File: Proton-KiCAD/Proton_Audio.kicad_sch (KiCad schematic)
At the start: 30 parts, among them J13 SJ-43514, J15 SPEAKER_OUT, U10 LM324, U9 LM386

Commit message: finished updated layout
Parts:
- J6: renamed from J13; footprint Custom_footprints:CUI_SJ-43514 -> Custom Footprints:CUI_SJ-43514
- renumbered C28 to C24, C22 to C25, C36 to C26, C37 to C27, C38 to C28, C23 to C29, C24 to C30, C39 to C31, C25 to C32, C40 to C33, C42 to C34, C43 to C35, J15 to J12, R44 to R19, R45 to R20, R25 to R22, R38 to R27, R39 to R28, R35 to R29, R15 to R30, R36 to R31, R26 to R32, R27 to R33, R37 to R34, R28 to R35, R42 to R38, U10 to U6, U9 to U7
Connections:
- net VGND is gone; now on net SGND: C26.2, C27.2, C29.2, C31.2, C32.2, R30.1
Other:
- moved on the sheet: C33, C34, C35, J12, R38, U7

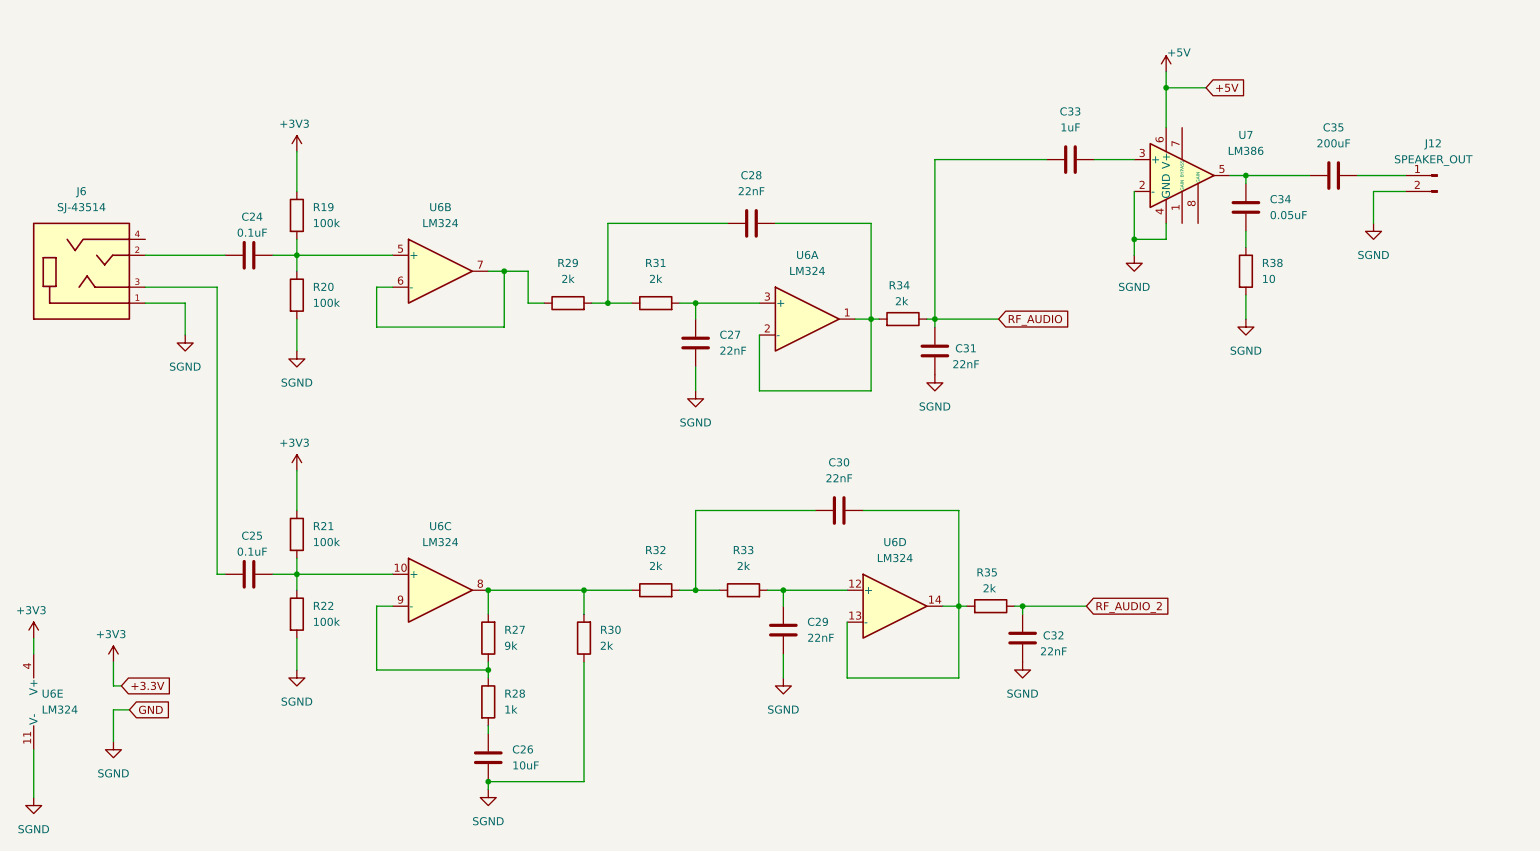
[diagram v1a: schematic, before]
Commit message: BOM and CPL changes
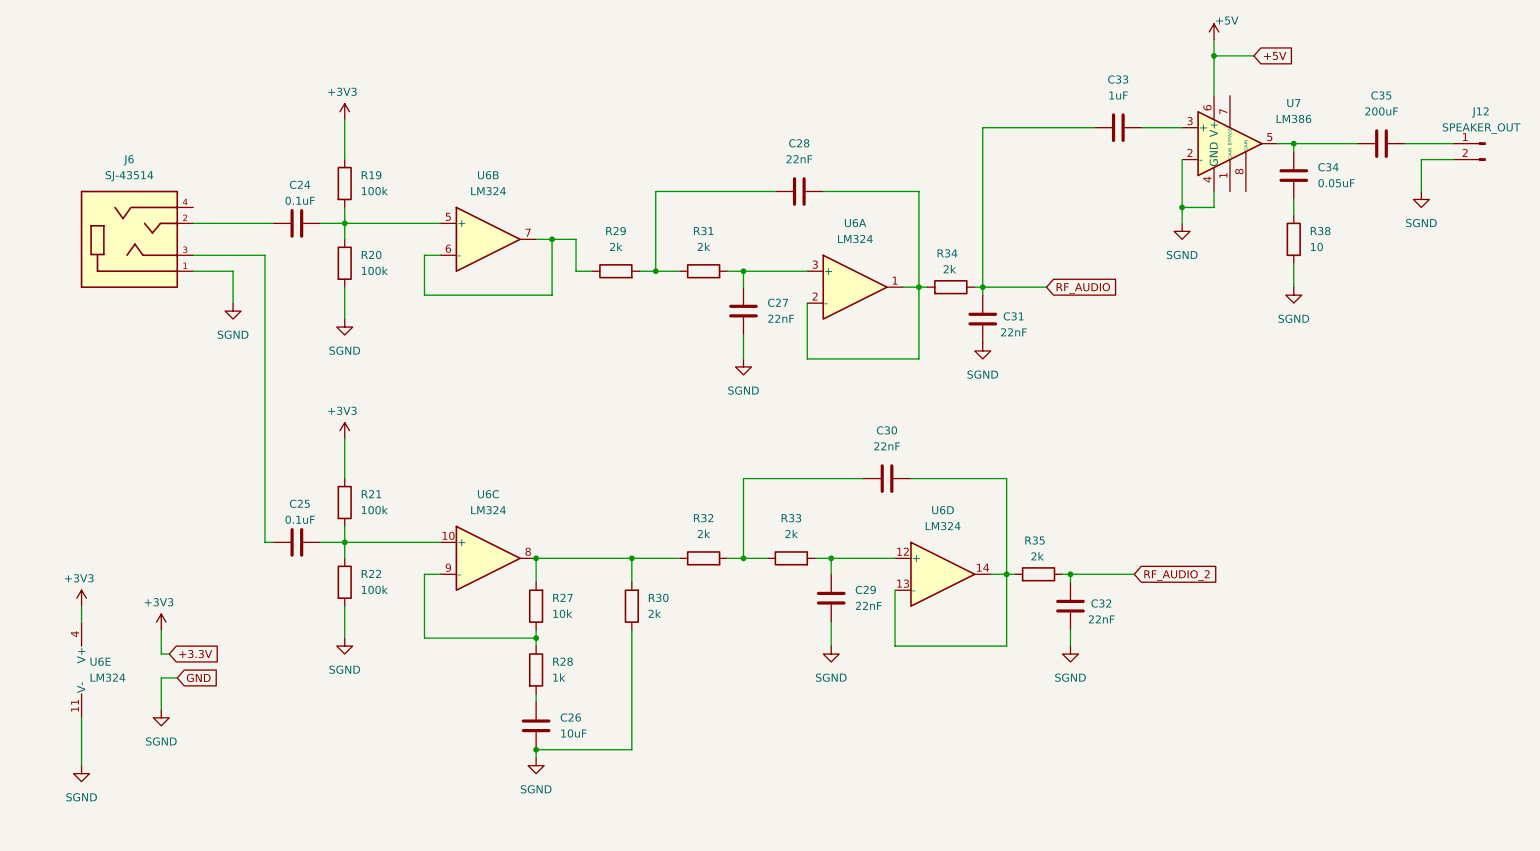
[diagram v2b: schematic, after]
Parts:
- R27: value 9k -> 10k
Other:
- moved on the sheet: C24, C25, C26, C27, C28, C29, C30, C31, C32, C33, C34, C35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

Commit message: changing for basic pedal
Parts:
- removed C24, C25: 0.1uF, Capacitor_SMD:C_0402_1005Metric, symbol Device:C
- removed C26: 10uF, Capacitor_SMD:C_0805_2012Metric, symbol Device:C
- removed C27, C28, C29, C30, C31, C32: 22nF, Capacitor_SMD:C_0402_1005Metric, symbol Device:C
- removed C33: 1uF, Capacitor_SMD:C_0402_1005Metric, symbol Device:C
- removed C34: 0.05uF, Capacitor_SMD:C_0402_1005Metric, symbol Device:C
- removed C35: 200uF, Capacitor_SMD:CP_Elec_6.3x4.5, symbol Device:C
- removed J12: SPEAKER_OUT, Connector_PinHeader_2.54mm:PinHeader_1x02_P2.54mm_Vertical, symbol Connector:Conn_01x02_Pin
- removed J6: SJ-43514, Custom Footprints:CUI_SJ-43514, symbol SJ-43514:SJ-43514
- removed R19, R20, R21, R22: 100k, Resistor_SMD:R_0402_1005Metric, symbol Device:R
- removed R27: 10k, Resistor_SMD:R_0402_1005Metric, symbol Device:R
- removed R28: 1k, Resistor_SMD:R_0402_1005Metric, symbol Device:R
- removed R29, R30, R31, R32, R33, R34, R35: 2k, Resistor_SMD:R_0402_1005Metric, symbol Device:R
- removed R38: 10, Resistor_SMD:R_0402_1005Metric, symbol Device:R
- removed U6: LM324, Package_DIP:DIP-14_W7.62mm, symbol Amplifier_Operational:LM324
- removed U7: LM386, Package_DIP:DIP-8_W7.62mm, symbol Amplifier_Audio:LM386
